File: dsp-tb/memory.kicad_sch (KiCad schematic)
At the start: 3 parts, among them J9 104031-0811, U6 IS42S16800F-7BL-TR, U7 IS25LP080D-JNLE

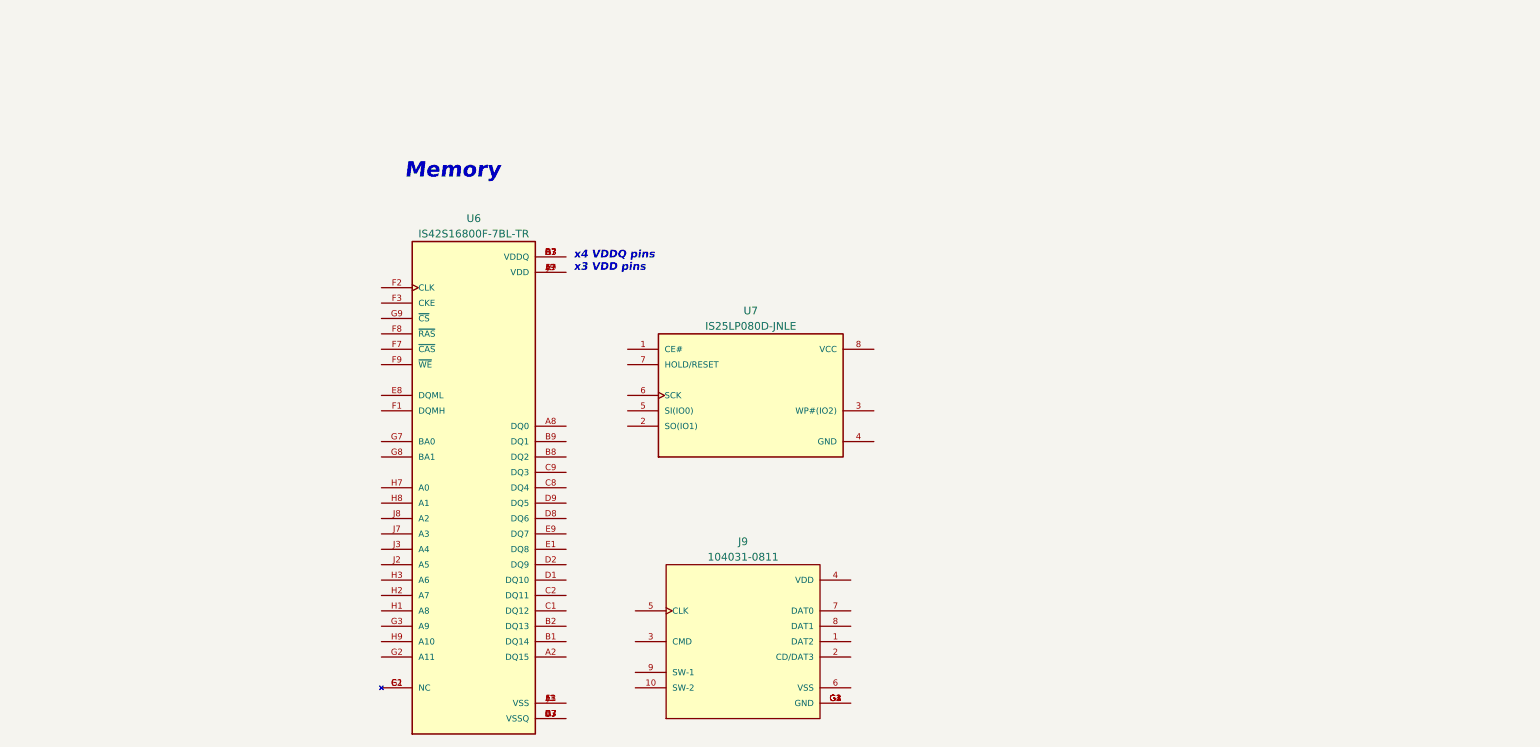
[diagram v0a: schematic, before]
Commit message: dsp-tb: finish schematic drawings
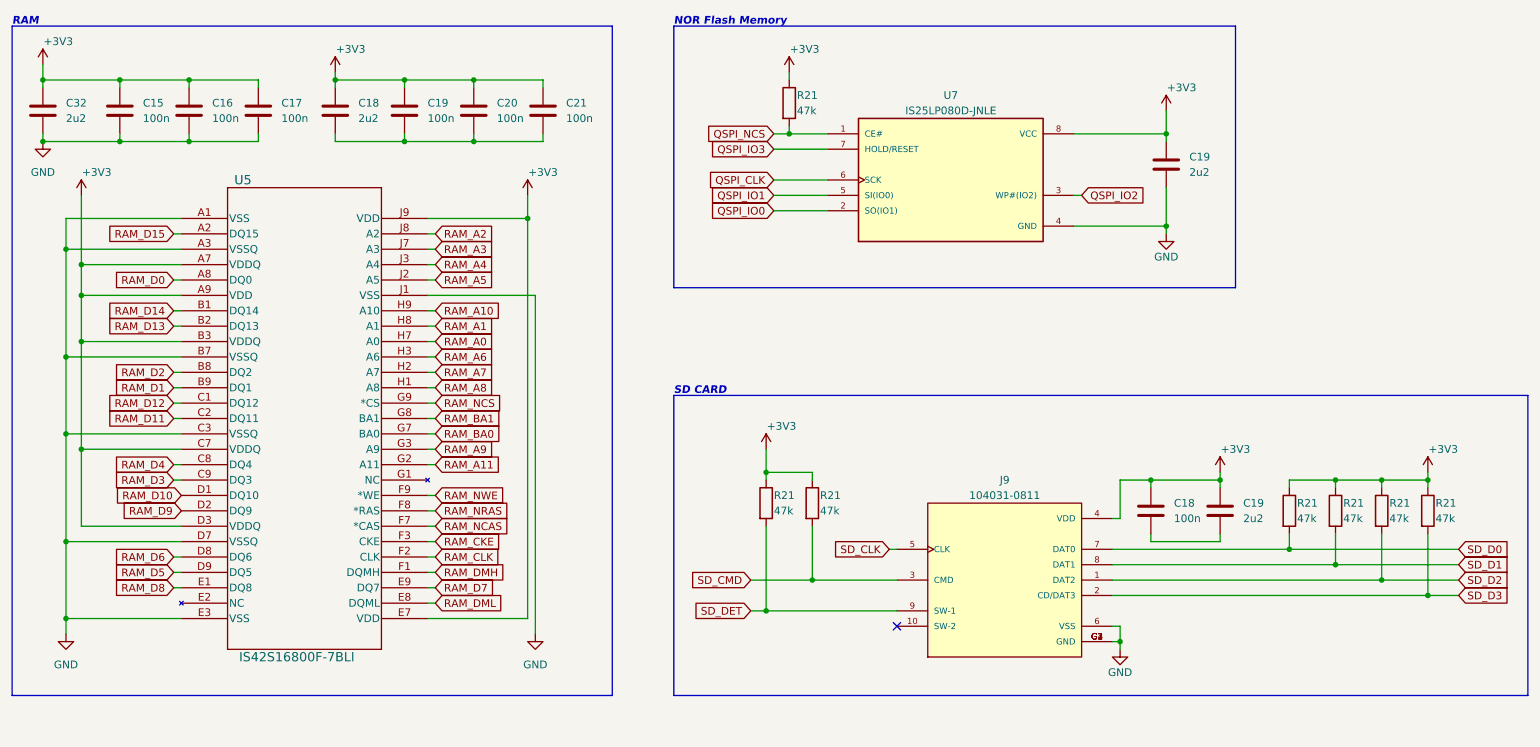
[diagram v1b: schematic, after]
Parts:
- removed U6: IS42S16800F-7BL-TR, footprints:BGA54C80P9X9_800X800X120, symbol IS42S16800F-7BL-TR:IS42S16800F-7BL-TR
- added C15, C16, C17, C18, C19, C20, C21: 100n, Capacitor_SMD:C_0402_1005Metric, symbol Device:C
- added C18, C19 (x2), C32: 2u2, Capacitor_SMD:C_0402_1005Metric, symbol Device:C
- added R21 (x7): 47k, Resistor_SMD:R_0402_1005Metric, symbol Device:R
- added U5: IS42S16800F-7BLI, footprints:BGA54C80P9X9_800X800X120, symbol IS42S16800F-7BLI:IS42S16800F-7BLI
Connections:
- net QSPI_NCS: now reaches U7.1 (CE#)
- net QSPI_NCS: now also R21.2
- net QSPI_IO0: now reaches U7.2 (SO(IO1))
- net QSPI_IO2: now reaches U7.3 (WP#(IO2))
- net GND: now reaches U7.4 (GND)
- net GND: now also J9.6 (VSS), J9.G1 (GND), J9.G2 (GND), J9.G3 (GND), J9.G4 (GND), C15.2, C16.2, C17.2, C19.2, C32.2, U5.A1 (VSS), U5.A3 (VSSQ), U5.B7 (VSSQ), U5.C3 (VSSQ), U5.D7 (VSSQ), U5.E3 (VSS), U5.J1 (VSS)
- net QSPI_IO1: now reaches U7.5 (SI(IO0))
- net QSPI_CLK: now reaches U7.6 (SCK)
- net QSPI_IO3: now reaches U7.7 (HOLD/RESET)
- net +3V3: now reaches U7.8 (VCC)
- net +3V3: now also J9.4 (VDD), C15.1, C16.1, C17.1, C18.1, C18.1, C19.1, C19.1, C19.1, C20.1, C21.1, C32.1, R21.1, R21.1, R21.1, R21.1, R21.1, R21.1, R21.1, U5.A7 (VDDQ), U5.A9 (VDD), U5.B3 (VDDQ), U5.C7 (VDDQ), U5.D3 (VDDQ), U5.E7 (VDD), U5.J9 (VDD)
- net SD_D2: now reaches J9.1 (DAT2)
- net SD_D2: now also R21.2
- net SD_D3: now reaches J9.2 (CD/DAT3)
- net SD_D3: now also R21.2
- net SD_CMD: now reaches J9.3 (CMD)
- net SD_CMD: now also R21.2
- net SD_CLK: now reaches J9.5 (CLK)
- net SD_D0: now reaches J9.7 (DAT0)
- net SD_D0: now also R21.2
- net SD_D1: now reaches J9.8 (DAT1)
- net SD_D1: now also R21.2
- net SD_DET: now reaches J9.9 (SW-1)
- net SD_DET: now also R21.2
- new net: C18.2, C19.2, C20.2, C21.2
- new net: C18.2, C19.2
- new net RAM_A0: U5.H7 (A0)
- new net RAM_A1: U5.H8 (A1)
- new net RAM_A10: U5.H9 (A10)
- new net RAM_A11: U5.G2 (A11)
- new net RAM_A2: U5.J8 (A2)
- new net RAM_A3: U5.J7 (A3)
- new net RAM_A4: U5.J3 (A4)
- new net RAM_A5: U5.J2 (A5)
- new net RAM_A6: U5.H3 (A6)
- new net RAM_A7: U5.H2 (A7)
- new net RAM_A8: U5.H1 (A8)
- new net RAM_A9: U5.G3 (A9)
- new net RAM_BA0: U5.G7 (BA0)
- new net RAM_BA1: U5.G8 (BA1)
- new net RAM_CKE: U5.F3 (CKE)
- new net RAM_CLK: U5.F2 (CLK)
- new net RAM_D0: U5.A8 (DQ0)
- new net RAM_D1: U5.B9 (DQ1)
- new net RAM_D10: U5.D1 (DQ10)
- new net RAM_D11: U5.C2 (DQ11)
- new net RAM_D12: U5.C1 (DQ12)
- new net RAM_D13: U5.B2 (DQ13)
- new net RAM_D14: U5.B1 (DQ14)
- new net RAM_D15: U5.A2 (DQ15)
- new net RAM_D2: U5.B8 (DQ2)
- new net RAM_D3: U5.C9 (DQ3)
- new net RAM_D4: U5.C8 (DQ4)
- new net RAM_D5: U5.D9 (DQ5)
- new net RAM_D6: U5.D8 (DQ6)
- new net RAM_D7: U5.E9 (DQ7)
- new net RAM_D8: U5.E1 (DQ8)
- new net RAM_D9: U5.D2 (DQ9)
- new net RAM_DMH: U5.F1 (DQMH)
- new net RAM_DML: U5.E8 (DQML)
- new net RAM_NCAS: U5.F7 (*CAS)
- new net RAM_NCS: U5.G9 (*CS)
- new net RAM_NRAS: U5.F8 (*RAS)
- new net RAM_NWE: U5.F9 (*WE)
- no-connect marks 0 -> 1
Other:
- note added: "NOR Flash Memory"
- note added: "RAM"
- note added: "SD CARD"
- note removed: "Memory"
- note removed: "x4 VDDQ pins x3 VDD pins"
- moved on the sheet: J9, U7
